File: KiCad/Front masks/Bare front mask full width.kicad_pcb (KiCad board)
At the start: 2 copper layers, 35 x 111.5 mm, 7 parts

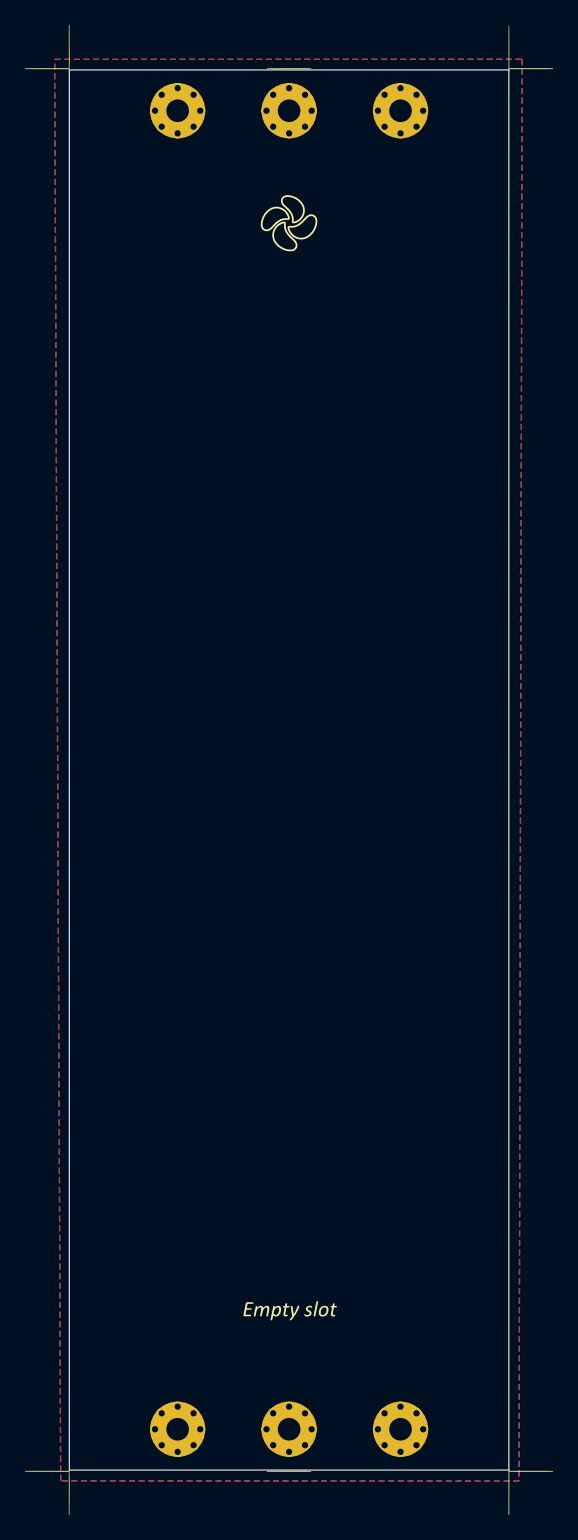
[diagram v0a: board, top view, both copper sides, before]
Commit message: Bare front masks resized
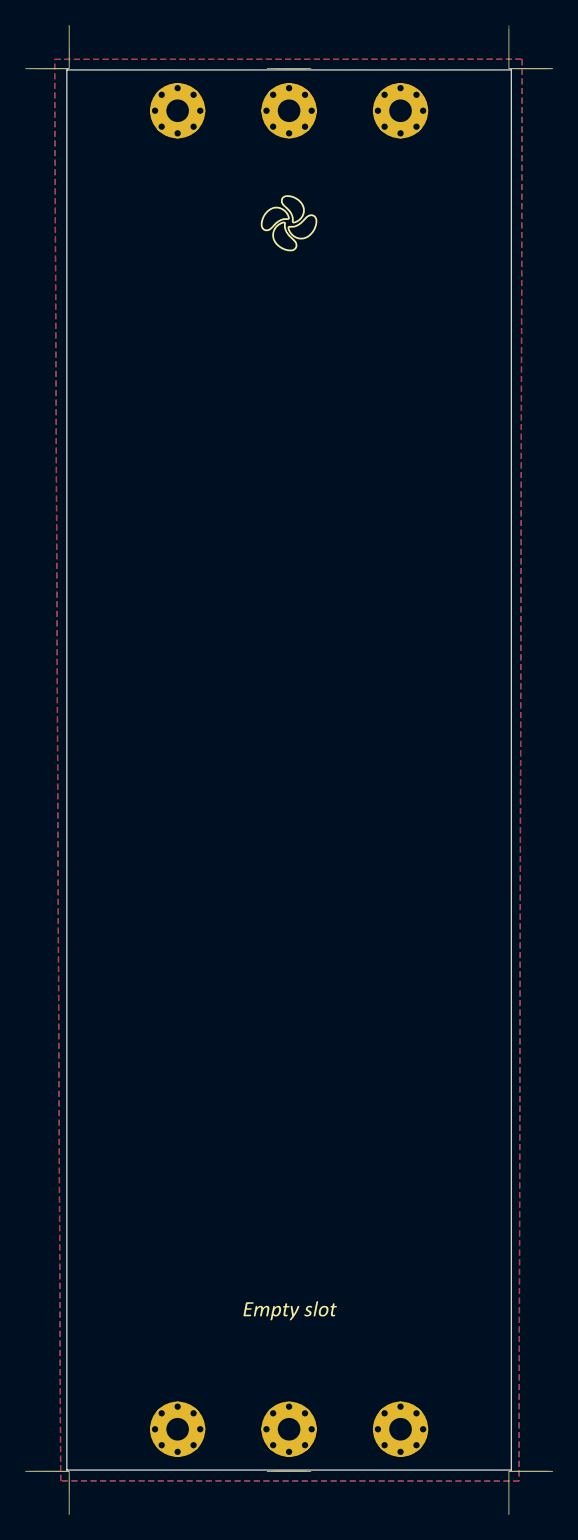
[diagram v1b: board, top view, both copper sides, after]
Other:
- board size 35 x 111.5 mm -> 35.4 x 111.5 mm
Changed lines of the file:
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@@
 		(grid_origin 140.5 150)
 		(pcbplotparams
-			(layerselection 0x00000000_00000000_55555555_57555577)
+			(layerselection 0x00000000_00000000_55555555_5755f57f)
 			(plot_on_all_layers_selection 0x00000000_00000000_00000000_00000000)
 			(disableapertmacros no)
@@
 	)
 	(gr_rect
-		(start 140.5 144)
-		(end 175.4 150)
+		(start 140.3 38.5)
+		(end 175.7 44.5)
 		(stroke
 			(width 0.1)
@@
 	)
 	(gr_rect
-		(start 140.52 38.5)
-		(end 175.42 44.5)
+		(start 140.3 144)
+		(end 175.7 150)
 		(stroke
 			(width 0.1)
@@
 		(layer "F.Paste")
 	)
-	(gr_line
-		(start 140.5 150)
-		(end 140.5 38.5)
+	(gr_rect
+		(start 140.3 38.5)
+		(end 175.7 44.5)
+		(stroke
+			(width 0.1)
+			(type solid)
+		)
+		(fill yes)
+		(layer "B.Paste")
+	)
+	(gr_rect
+		(start 140.3 144)
+		(end 175.7 150)
+		(stroke
+			(width 0.1)
+			(type solid)
+		)
+		(fill yes)
+		(layer "B.Paste")
+	)
+	(gr_rect
+		(start 140.3 38.5)
+		(end 175.7 150)
 		(stroke
 			(width 0.05)
-			(type solid)
-		)
-		(locked yes)
-		(layer "Edge.Cuts")
-	)
-	(gr_line
-		(start 175.5 38.5)
-		(end 140.5 38.5)
-		(stroke
-			(width 0.05)
-			(type solid)
-		)
-		(locked yes)
-		(layer "Edge.Cuts")
-	)
-	(gr_line
-		(start 175.5 38.5)
-		(end 175.5 150)
-		(stroke
-			(width 0.05)
-			(type solid)
-		)
-		(locked yes)
-		(layer "Edge.Cuts")
-	)
-	(gr_line
-		(start 175.5 150)
-		(end 140.5 150)
-		(stroke
-			(width 0.05)
-			(type solid)
-		)
-		(locked yes)
+			(type default)
+		)
+		(fill no)
 		(layer "Edge.Cuts")
 	)
@@
 		(layer "User.1")
 		(pts
-			(xy 140.5 152.074999) (xy 175.5 152.05)
+			(xy 140.3 150) (xy 175.740466 150.063136)
 		)
 		(height 2.5375)
@@
 			(keep_text_aligned yes)
 		)
-		(gr_text "35,0 mm"
-			(at 158 153.462499 0)
+		(gr_text "35,4 mm"
+			(at 158.020233 151.3875 0)
 			(layer "User.1")
 			(effects
@@
 		)
 		(min_thickness 0.25)
-		(fill
+		(fill yes
 			(thermal_gap 0.5)
 			(thermal_bridge_width 0.5)
@@
 		)
 	)
-	(group ""
-		(locked yes)
-		(members "3bec24fe-9634-410f-ae22-abe963cd70e2" "40c1de93-adce-49ae-ba59-9ddb6a63c44d"
-			"b76af28c-8a19-4f35-81c9-1c72619257bb" "bed9b981-e39a-48df-83b7-bc13756cdbbc"
-		)
-	)
